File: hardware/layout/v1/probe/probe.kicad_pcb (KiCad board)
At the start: 4 copper layers, 14 x 56 mm, 22 parts, among them J1 Main board, J2 Reflector T-Socket SMD, Q1 AO3400A, U1 SCD41-D-R2, U2 SGP41-D-R4, U3 SHT40-AD1F-R2, U4 LM2903DR2G, U5 BMP585

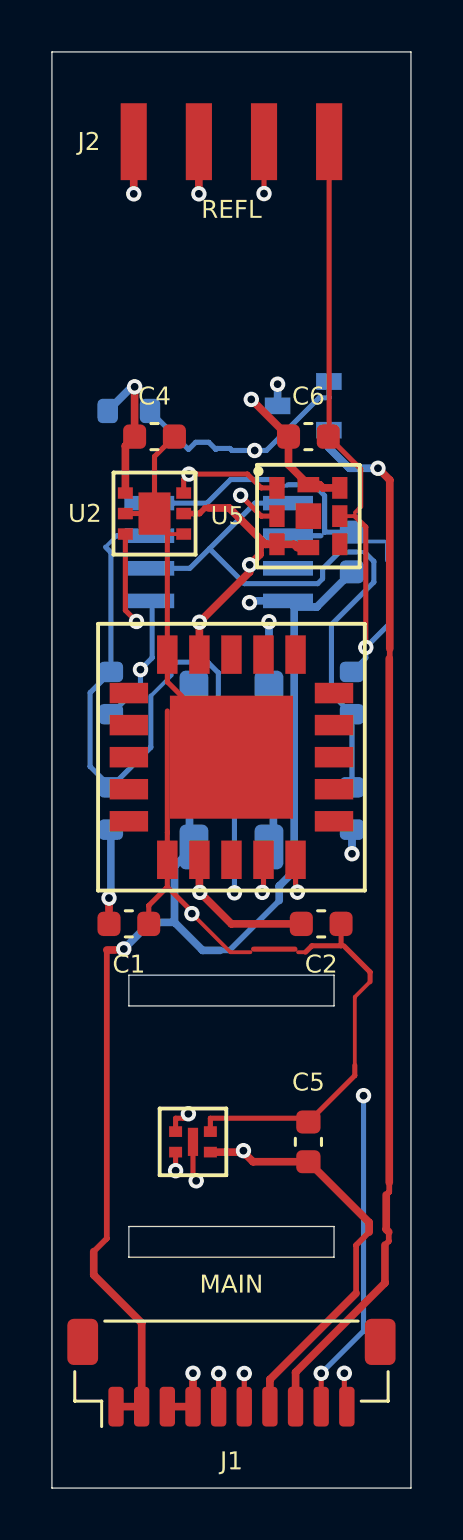
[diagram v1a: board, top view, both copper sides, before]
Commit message: Update AGENTS.md, CALIBRATION.md, and README.md for PTFE dome diffuser, probe heater setpoint change to −7.6 °C, crown preamp bias mode, RS-485 fail-safe bias note, and enclosure seal test
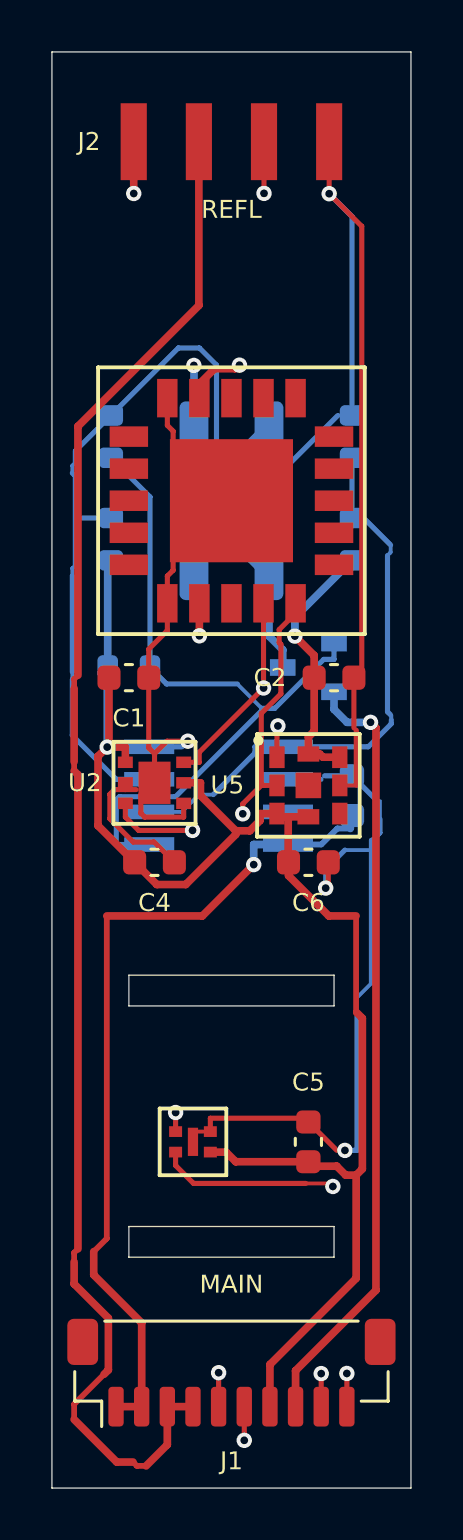
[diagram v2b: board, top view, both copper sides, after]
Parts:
- R5: value 22k -> 51k
- moved C4 16.6 mm to (4.00, -24.4)
- moved C6 16.6 mm to (10.0, -24.4)
- moved R1 10.5 mm to (7.00, -35.5)
- moved R2 10.5 mm to (7.00, -41.5)
- moved R3 10.5 mm to (2.30, -37.0)
- moved R4 10.5 mm to (11.7, -37.0)
- moved TH1 10.5 mm to (7.00, -38.5)
- moved U2 10.5 mm to (4.00, -27.5)
- moved U5 10.5 mm to (10.0, -27.4)
- moved Q1 10.2 mm to (10.0, -32.0)
- moved R5 10.0 mm to (11.7, -41.0)
- moved R6 10.0 mm to (3.00, -32.0)
- moved R7 10.0 mm to (2.30, -41.0)
- moved U1 10.0 mm to (7.00, -38.5)
- moved C2 9.61 mm to (11.0, -31.6)
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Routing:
- net I2C_SDA: track 73.7 -> 48.2 mm, vias 6 -> 4
- net I2C_SCL: track 59.3 -> 47.5 mm
- net CO2_HEAT_RTN: track 41.3 -> 30.4 mm
- net CO2_HEAT_SW: track 19.5 -> 10.9 mm, vias 2 -> 0
- net GND: track 87.5 -> 95.7 mm
- net HEAT_SW: track 54.3 -> 60.3 mm, vias 2 -> 0
- net CO2_NTC: track 23.8 -> 29.2 mm
- net +12V_HEAT: track 81.4 -> 76.2 mm
- net CO2_GATE: track 25.5 -> 28.3 mm, vias 2 -> 0
- net CO2_VSET: track 24.1 -> 22.4 mm
- net +3V3_PROBE: track 95.4 -> 94.3 mm, vias 8 -> 4
- net NTC_SENSE: track 57.2 -> 58.0 mm
